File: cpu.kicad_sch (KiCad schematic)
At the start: 30 parts, among them Q1 К315А, SW1 УСТ, Y1 32768 Hz, Y2 16 Mhz

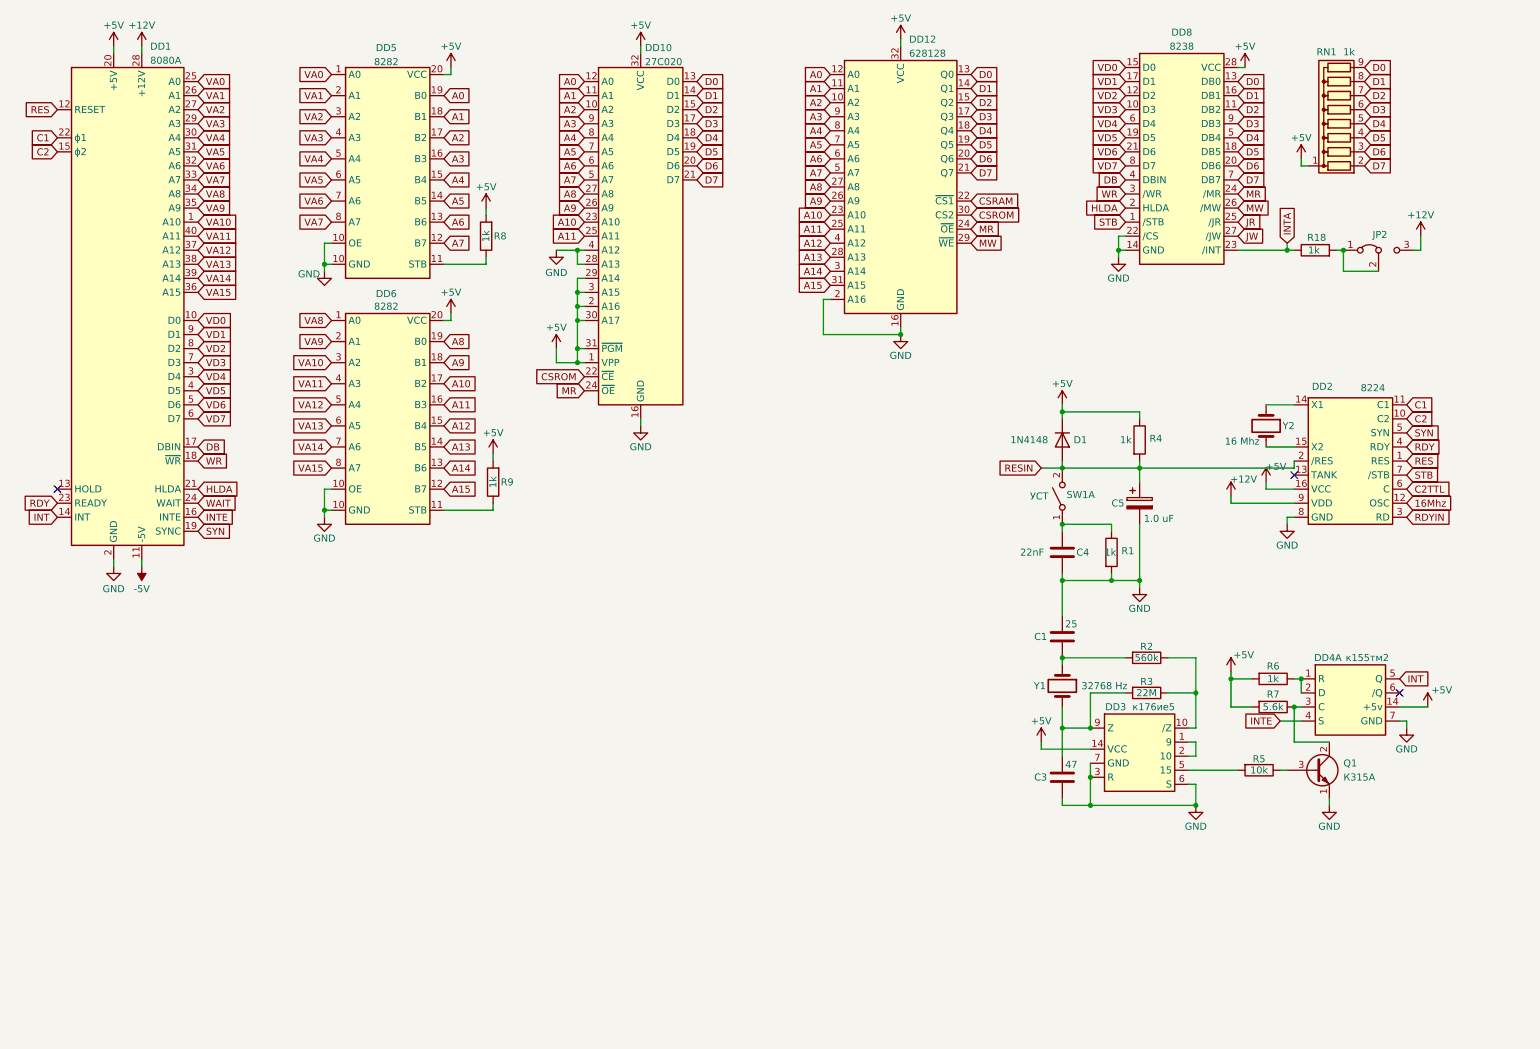
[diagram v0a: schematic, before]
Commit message: full rework. ic numbers now same as in original schema
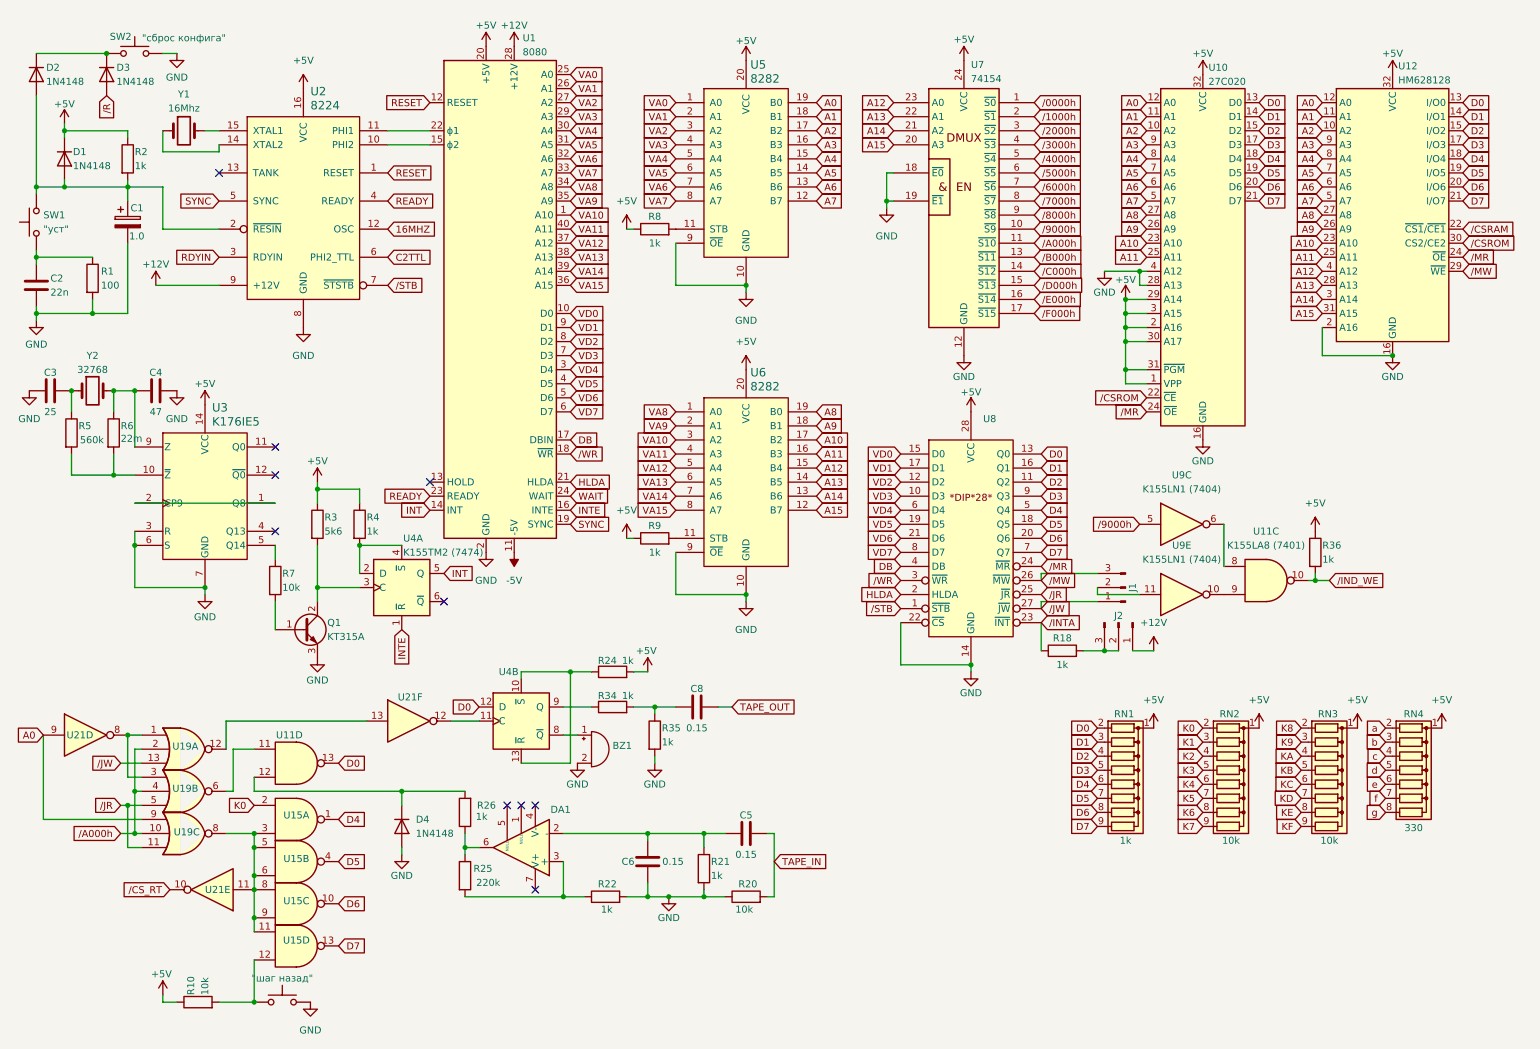
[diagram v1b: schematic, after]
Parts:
- removed C1: 25, Capacitor_THT:C_Axial_L3.8mm_D2.6mm_P7.50mm_Horizontal, symbol Device:C
- removed C5: 1.0 uF, Capacitor_THT:CP_Radial_D4.0mm_P1.50mm, symbol Device:C_Polarized
- removed D1: 1N4148, Diode_THT:D_DO-35_SOD27_P7.62mm_Horizontal, symbol Diode:1N4148
- removed DD1: 8080A, Package_DIP:DIP-40_W15.24mm, symbol MCU_Intel:8080A
- removed DD10: 27C020, Package_DIP:DIP-32_W15.24mm_LongPads, symbol Memory_EPROM:27C020
- removed DD12: 628128, Package_DIP:DIP-32_W15.24mm_LongPads, symbol Memory_RAM:628128_DIP32_SSOP32
- removed DD2: 8224, Package_DIP:CERDIP-16_W7.62mm_SideBrazed_LongPads, symbol intel:8224
- removed DD3: к176ие5, Package_DIP:DIP-14_W7.62mm_LongPads, symbol cccp:к176ие5
- removed DD4: к155тм2, Package_DIP:DIP-14_W7.62mm_LongPads, symbol 74xx_IEEE:7474
- removed DD5, DD6: 8282, Package_DIP:DIP-20_W7.62mm_LongPads, symbol intel:8282
- removed DD8: 8238, Package_DIP:DIP-28_W7.62mm_LongPads, symbol intel:8238
- removed JP2: ~, symbol Jumper:Jumper_3_Bridged12
- removed Q1: К315А, Package_TO_SOT_THT:TO-18-3_Window, symbol Transistor_BJT:BF459
- removed SW1: УСТ, symbol Switch:SW_DPST_x2
- added BZ1: ~, symbol Device:Buzzer
- added C1: 1.0, Capacitor_THT:CP_Radial_D4.0mm_P1.50mm, symbol Device:C_Polarized
- added C2: 22n, Capacitor_THT:C_Radial_D5.0mm_H5.0mm_P2.00mm, symbol Device:C
- added C5, C6, C8: 0.15, Capacitor_THT:C_Radial_D5.0mm_H5.0mm_P2.00mm, symbol Device:C
- added D1, D2, D3: 1N4148, Diode_THT:D_5KPW_P12.70mm_Horizontal, symbol Device:D
- added D4: 1N4148, Diode_THT:D_DO-35_SOD27_P7.62mm_Horizontal, symbol Diode:1N4148
- added DA1: TL081, symbol Amplifier_Operational:TL081
- added J1, J2: ~, Connector_PinSocket_2.54mm:PinSocket_1x03_P2.54mm_Vertical, symbol Connector:Conn_01x03_Pin
- added Q1: KT315A, Package_TO_SOT_THT:TO-39-3, symbol Transistor_BJT:2SD1047
- added R10, R20: 10k, Resistor_THT:R_Axial_DIN0204_L3.6mm_D1.6mm_P5.08mm_Horizontal, symbol Device:R
- added R21, R22, R24, R26, R34, R35, R36: 1k, Resistor_THT:R_Axial_DIN0204_L3.6mm_D1.6mm_P5.08mm_Horizontal, symbol Device:R
- added R25: 220k, Resistor_THT:R_Axial_DIN0204_L3.6mm_D1.6mm_P5.08mm_Horizontal, symbol Device:R
- added RN2, RN3: 10k, Resistor_THT:R_Array_SIP9, symbol Device:R_Network08
- added RN4: 330, Resistor_THT:R_Array_SIP8, symbol Device:R_Network07
- added SW1: "уст", symbol Switch:SW_Push
- added SW19: "шаг назад", symbol Switch:SW_Push
- added SW2: "сброс конфига", symbol Switch:SW_Push
- added U1: 8080, Package_DIP:DIP-40_W15.24mm, symbol MCU_Intel:8080
- added U10: 27C020, symbol Memory_EPROM:27C020
- added U11, U15: K155LA8 (7401), Package_DIP:DIP-14_W7.62mm, symbol 74xx:74LS01
- added U12: HM628128, Package_DIP:DIP-32_W15.24mm_LongPads, symbol Memory_RAM:HM628128_DIP32_SOP32
- added U19: K155LE4 (7427), Package_DIP:DIP-14_W7.62mm, symbol 74xx:74LS27
- added U2: 8224, *DIP*16*, symbol User:8224
- added U21: K155LN1 (7404), Package_DIP:DIP-14_W7.62mm_LongPads, symbol 74xx:74LS04
- added U3: K176IE5, symbol User:K176IE5
- added U4: K155TM2 (7474), Package_DIP:DIP-14_W7.62mm, symbol 74xx:74LS74
- added U5, U6: 8282, *DIP*20*, symbol User:8282
- added U7: 74154, Package_DIP:DIP-24_18.0mmx34.29mm_W15.24mm_LongPads, symbol 74xx_IEEE:74154
- added U8: ~, symbol User:8238
- added U9: K155LN1 (7404), Package_DIP:DIP-14_W7.62mm, symbol 74xx:74LS04
- C3: value 47 -> 25; footprint Capacitor_THT:C_Axial_L3.8mm_D2.6mm_P7.50mm_Horizontal -> Capacitor_THT:C_Radial_D5.0mm_H5.0mm_P2.00mm
- C4: value 22nF -> 47; footprint Capacitor_THT:C_Axial_L3.8mm_D2.6mm_P7.50mm_Horizontal -> Capacitor_THT:C_Radial_D5.0mm_H5.0mm_P2.00mm
- R1: value 1k -> 100
- R2: value 560k -> 1k
- R3: value 22M -> 5k6
- R5: value 10k -> 560k
- R6: value 1k -> 22m
- R7: value 5.6k -> 10k
- Y1: value 32768 Hz -> 16Mhz; footprint (none) -> Crystal:Crystal_HC49-U_Vertical
- Y2: value 16 Mhz -> 32768; footprint (none) -> Crystal:Crystal_HC49-U_Vertical
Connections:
- net +12V: now also J2.1 (Pin_1), U1.28 (+12V), U2.9 (+12V)
- net +5V: now also R2.1, R3.1, R8.1, R9.1, D1.1 (K), R10.1, R24.2, R36.1, RN2.1 (common), RN3.1 (common), RN4.1 (common), U1.20 (+5V), U10.1 (VPP), U10.2 (A16), U10.29 (A14), U10.3 (A15), U10.30 (A17), U10.31 (~{PGM}), U10.32 (VCC), U12.32 (VCC), U2.16 (VCC), U3.14 (VCC), U5.20 (VCC), U6.20 (VCC), U7.24 (VCC), U8.28 (VCC); no longer R6.2, R7.2, R8.2, R9.2
- net -5V: now also U1.11 (-5V)
- net A0: now also U10.12 (A0), U12.12 (A0), U19.9, U21.9, U5.19 (B0)
- net A1: now also U10.11 (A1), U12.11 (A1), U5.18 (B1)
- net A10: now also U10.23 (A10), U12.23 (A10), U6.17 (B2)
- net A11: now also U10.25 (A11), U12.25 (A11), U6.16 (B3)
- net A12: now also U12.4 (A12), U6.15 (B4), U7.23 (A0)
- net A13: now also U12.28 (A13), U6.14 (B5), U7.22 (A1)
- net A14: now also U12.3 (A14), U6.13 (B6), U7.21 (A2)
- net A15: now also U12.31 (A15), U6.12 (B7), U7.20 (A3)
- net A2: now also U10.10 (A2), U12.10 (A2), U5.17 (B2)
- net A3: now also U10.9 (A3), U12.9 (A3), U5.16 (B3)
- net A4: now also U10.8 (A4), U12.8 (A4), U5.15 (B4)
- net A5: now also U10.7 (A5), U12.7 (A5), U5.14 (B5)
- net A6: now also U10.6 (A6), U12.6 (A6), U5.13 (B6)
- net A7: now also U10.5 (A7), U12.5 (A7), U5.12 (B7)
- net A8: now also U10.27 (A8), U12.27 (A8), U6.19 (B0)
- net A9: now also U10.26 (A9), U12.26 (A9), U6.18 (B1)
- net C2TTL: now also U2.6 (PHI2_TTL)
- net D0: now also RN1.2 (R1), U10.13 (D0), U11.13, U12.13 (I/O0), U4.12 (D), U8.13 (Q0); no longer RN1.9 (R8)
- net D1: now also RN1.3 (R2), U10.14 (D1), U12.14 (I/O1), U8.16 (Q1); no longer RN1.8 (R7)
- net D2: now also RN1.4 (R3), U10.15 (D2), U12.15 (I/O2), U8.11 (Q2); no longer RN1.7 (R6)
- net D3: now also RN1.5 (R4), U10.17 (D3), U12.17 (I/O3), U8.9 (Q3); no longer RN1.6 (R5)
- net D4: now also RN1.6 (R5), U10.18 (D4), U12.18 (I/O4), U15.1, U8.5 (Q4); no longer RN1.5 (R4)
- net D5: now also RN1.7 (R6), U10.19 (D5), U12.19 (I/O5), U15.4, U8.18 (Q5); no longer RN1.4 (R3)
- net D6: now also RN1.8 (R7), U10.20 (D6), U12.20 (I/O6), U15.10, U8.20 (Q6); no longer RN1.3 (R2)
- net D7: now also RN1.9 (R8), U10.21 (D7), U12.21 (I/O7), U15.13, U8.7 (Q7); no longer RN1.2 (R1)
- net DB: now also U1.17 (DBIN), U8.4 (DB)
- net GND: now also C3.1, BZ1.2 (-), C1.2, C2.2, C6.2, D4.2 (A), Q1.3 (E), R20.1, R21.2, R22.2, R35.2, SW19.2, SW2.2, U1.2 (GND), U10.16 (GND), U10.28 (A13), U10.4 (A12), U12.16 (GND), U12.2 (A16), U2.8 (GND), U3.3 (R), U3.6 (S), U3.7 (GND), U5.10 (GND), U5.9 (~{OE}), U6.10 (GND), U6.9 (~{OE}), U7.12 (GND), U7.18 (~{E0}), U7.19 (~{E1}), U8.14 (GND), U8.22 (~{CS}); no longer C3.2
- net HLDA: now also U1.21 (HLDA), U8.2 (HLDA)
- net INT: now also U1.14 (INT), U4.5 (Q)
- net INTE: now also U1.16 (INTE), U4.1 (~{R})
- net RDYIN: now also U2.3 (RDYIN)
- net VA0: now also U1.25 (A0), U5.1 (A0)
- net VA1: now also U1.26 (A1), U5.2 (A1)
- net VA10: now also U1.1 (A10), U6.3 (A2)
- net VA11: now also U1.40 (A11), U6.4 (A3)
- net VA12: now also U1.37 (A12), U6.5 (A4)
- net VA13: now also U1.38 (A13), U6.6 (A5)
- net VA14: now also U1.39 (A14), U6.7 (A6)
- net VA15: now also U1.36 (A15), U6.8 (A7)
- net VA2: now also U1.27 (A2), U5.3 (A2)
- net VA3: now also U1.29 (A3), U5.4 (A3)
- net VA4: now also U1.30 (A4), U5.5 (A4)
- net VA5: now also U1.31 (A5), U5.6 (A5)
- net VA6: now also U1.32 (A6), U5.7 (A6)
- net VA7: now also U1.33 (A7), U5.8 (A7)
- net VA8: now also U1.34 (A8), U6.1 (A0)
- net VA9: now also U1.35 (A9), U6.2 (A1)
- net VD0: now also U1.10 (D0), U8.15 (D0)
- net VD1: now also U1.9 (D1), U8.17 (D1)
- net VD2: now also U1.8 (D2), U8.12 (D2)
- net VD3: now also U1.7 (D3), U8.10 (D3)
- net VD4: now also U1.3 (D4), U8.6 (D4)
- net VD5: now also U1.4 (D5), U8.19 (D5)
- net VD6: now also U1.5 (D6), U8.21 (D6)
- net VD7: now also U1.6 (D7), U8.8 (D7)
- net WAIT: now also U1.24 (WAIT)
- net at C4.1: now also R6.1, Y2.2, U3.9 (Z); no longer R1.1
- net at R2.2: now also C1.1, D1.2 (A), D2.2 (A), SW1.2, U2.2 (~{RESIN}); no longer Y1.1
- net at R7.1: now also U3.5 (Q14)
- net at R5.1: now also C3.2, Y2.1
- net at R5.2: now also R6.2, U3.10 (~{Z})
- net at R18.2: now also J2.2 (Pin_2), J2.3 (Pin_3)
- net INTA renamed /INTA
- net /INTA: now also U8.23 (~{INT})
- net RESIN: no longer names the net of R4.2
- net RESIN: now also U4.2 (D), U4.4 (~{S})
- new net: DA1.6, R25.1, R26.1
- new net: D4.1 (K), R26.2, U11.12
- new net: R8.2, U5.11 (STB)
- new net: J1.2 (Pin_2), U9.11
- new net: C5.1, C6.1, DA1.2 (-), R21.1
- new net: D2.1 (K), D3.1 (K), SW2.1
- new net: Q1.2 (C), R3.2, U4.3 (C)
- new net: U19.1, U19.3, U21.8
- new net: U1.15 (ϕ2), U2.10 (PHI2)
- new net: U1.22 (ϕ1), U2.11 (PHI1)
- new net: Q1.1 (B), R7.2
- new net: R10.2, SW19.1, U15.12
- new net: DA1.3 (+), R22.1, R25.2
- new net: BZ1.1 (+), U4.8 (~{Q})
- new net: U3.1 (Q8), U3.2 (CP9)
- new net: U11.11, U19.6
- new net: R9.2, U6.11 (STB)
- new net: C8.1, R34.2, R35.1
- new net: R24.1, U4.10 (~{S}), U4.13 (~{R})
- new net: U15.11, U15.3, U15.5, U15.6, U15.8, U15.9, U19.8, U21.11
- new net: U2.14 (XTAL2), Y1.1
- new net: U2.15 (XTAL1), Y1.2
- new net: U11.8, U9.6
- new net: U11.9, U9.10
- new net: U21.12, U4.11 (C)
- new net: U19.12, U21.13
- new net: R34.1, U4.9 (Q)
- new net: C2.1, R1.1, SW1.1
- new net 16MHZ: U2.12 (OSC)
- new net K0: RN2.2 (R1), U15.2
- new net K1: RN2.3 (R2)
- new net K2: RN2.4 (R3)
- new net K3: RN2.5 (R4)
- new net K4: RN2.6 (R5)
- new net K5: RN2.7 (R6)
- new net K6: RN2.8 (R7)
- new net K7: RN2.9 (R8)
- new net K8: RN3.2 (R1)
- new net K9: RN3.3 (R2)
- new net KA: RN3.4 (R3)
- new net KB: RN3.5 (R4)
- new net KC: RN3.6 (R5)
- new net KD: RN3.7 (R6)
- new net KE: RN3.8 (R7)
- new net KF: RN3.9 (R8)
- new net READY: U1.23 (READY), U2.4 (READY)
- new net RESET: U1.12 (RESET), U2.1 (RESET)
- new net SYNC: U1.19 (SYNC), U2.5 (SYNC)
- new net TAPE_IN: C5.2, R20.2
- new net TAPE_OUT: C8.2
- new net a: RN4.2 (R1)
- new net b: RN4.3 (R2)
- new net c: RN4.4 (R3)
- new net d: RN4.5 (R4)
- new net e: RN4.6 (R5)
- new net f: RN4.7 (R6)
- new net g: RN4.8 (R7)
- new net /0000h: U7.1 (~{S0})
- new net /1000h: U7.2 (~{S1})
- new net /2000h: U7.3 (~{S2})
- new net /3000h: U7.4 (~{S3})
- new net /4000h: U7.5 (~{S4})
- new net /5000h: U7.6 (~{S5})
- new net /6000h: U7.7 (~{S6})
- new net /7000h: U7.8 (~{S7})
- new net /8000h: U7.9 (~{S8})
- new net /9000h: U7.10 (~{S9}), U9.5
- new net /A000h: U19.10, U19.2, U19.4, U7.11 (~{S10})
- new net /B000h: U7.13 (~{S11})
- new net /C000h: U7.14 (~{S12})
- new net /CSRAM: U12.22 (~{CS1}/~{CE1})
- new net /CSROM: U10.22 (~{CE}), U12.30 (CS2/CE2)
- new net /CS_RT: U21.10
- new net /D000h: U7.15 (~{S13})
- new net /E000h: U7.16 (~{S14})
- new net /F000h: U7.17 (~{S15})
- new net /IND_WE: R36.2, U11.10
- new net /JR: U19.11, U19.5, U8.25 (~{JR})
- new net /JW: J1.1 (Pin_1), U19.13, U8.27 (~{JW})
- new net /MR: U10.24 (~{OE}), U12.24 (~{OE}), U8.24 (~{MR})
- new net /MW: J1.3 (Pin_3), U12.29 (~{WE}), U8.26 (~{MW})
- new net /R: D3.2 (A)
- new net /STB: U2.7 (~{STSTB}), U8.1 (~{STB})
- new net /WR: U1.18 (~{WR}), U8.3 (~{WR})
- no-connect marks 3 -> 10
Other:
- company: (none) -> Eugene Chertikhin
- title: (none) -> ЮТ-88

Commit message: footprints
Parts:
- RN2, RN3: footprint Resistor_THT:R_Array_SIP9 -> Resistor_THT:R_Axial_DIN0204_L3.6mm_D1.6mm_P5.08mm_Horizontal
- U1: value 8080 -> 580ВМ80; footprint Package_DIP:DIP-40_W15.24mm -> Package_DIP:DIP-40_W15.24mm_LongPads; Analog (none) -> 8080
- U11, U15: value K155LA8 (7401) -> K155ЛА8; footprint Package_DIP:DIP-14_W7.62mm -> Package_DIP:DIP-14_W7.62mm_LongPads; Analog (none) -> 7401
- U19: value K155LE4 (7427) -> K155ЛЕ4; footprint Package_DIP:DIP-14_W7.62mm -> Package_DIP:DIP-14_W7.62mm_LongPads; Analog (none) -> 7427
- U2: value 8224 -> 580ГФ24; footprint *DIP*16* -> Package_DIP:DIP-16_W7.62mm_LongPads; Analog (none) -> 8224
- U21: value K155LN1 (7404) -> K155ЛН1; Analog (none) -> 7404
- U3: value K176IE5 -> K176ИЕ5; footprint (none) -> Package_DIP:DIP-14_W7.62mm_LongPads; Analog (none) -> CD4033Е
- U4: value K155TM2 (7474) -> K155ТМ2; footprint Package_DIP:DIP-14_W7.62mm -> Package_DIP:DIP-14_W7.62mm_LongPads; Analog (none) -> 7474
- U5, U6: value 8282 -> 580ИР82; footprint *DIP*20* -> Package_DIP:DIP-20_W7.62mm_LongPads; Analog (none) -> 8282
- U7: value 74154 -> 155ИД3; Analog (none) -> 74154
- U9: value K155LN1 (7404) -> K155ЛН1; footprint Package_DIP:DIP-14_W7.62mm -> Package_DIP:DIP-14_W7.62mm_LongPads; Analog (none) -> 7404
- Y2: value 32768 -> 32768kHz
